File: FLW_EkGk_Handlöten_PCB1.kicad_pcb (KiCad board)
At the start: 2 copper layers, 120 x 60 mm, 72 parts, among them J10 Conn_01x02, J11 Conn_01x02, J12 Conn_01x02, J13 Conn_01x02, Q1 2SC4213, Q2 2N7002, Q60 2N7002, Q61 2N7002, Q62 2N7002, Q63 2N7002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

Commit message: continued
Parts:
- added LED66: SMLP36RGBNW3, NiksKiCadLibrary:LED_SMLP36_ROM, F.Cu at (104.9, 97.8)
- added LED67: SMLP36RGBNW3, NiksKiCadLibrary:LED_SMLP36_ROM, F.Cu at (104.9, 101.2)
- added R66: R, Resistor_SMD:R_1206_3216Metric, F.Cu at (101.6, 92.0)
- added R67: R, Resistor_SMD:R_1206_3216Metric, F.Cu at (104.8, 92.0)
- added R68: R, Resistor_SMD:R_1206_3216Metric, F.Cu at (108.1, 92.0)
- added R69: R, Resistor_SMD:R_1206_3216Metric, F.Cu at (101.6, 106.8)
- added R70: R, Resistor_SMD:R_1206_3216Metric, F.Cu at (104.8, 106.8)
- added R71: R, Resistor_SMD:R_1206_3216Metric, F.Cu at (108.1, 106.8)
- moved Q63 68.9 mm to (144.9, 94.8)
- moved Q64 68.5 mm to (144.9, 100.0)
- moved Q65 68.1 mm to (144.9, 105.1)
- moved Q60 57.4 mm to (139.5, 94.8)
- moved Q61 57.1 mm to (139.5, 100.0)
- moved Q62 56.8 mm to (139.5, 105.1)
- moved J13 46.1 mm to (99.5, 81.3), turned to 180 degrees
- moved J12 46.0 mm to (99.5, 74.9), turned to 180 degrees
- moved J11 46.0 mm to (99.5, 68.6), turned to 180 degrees
- moved J10 46.0 mm to (99.5, 62.2), turned to 180 degrees
- moved LED65 44.9 mm to (119.8, 97.0), turned to 150 degrees
- moved R62 44.8 mm to (130.5, 99.0), turned to -120 degrees
- moved R65 44.5 mm to (116.7, 99.5), turned to 60 degrees
- moved R61 44.2 mm to (126.9, 93.1), turned to -60 degrees
- moved R63 40.6 mm to (127.3, 105.1), turned to 180 degrees
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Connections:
- R60 pad 1: unconnected-(R60-Pad1) -> /Praxis 2/VDD_5V
- R61 pad 1: unconnected-(R61-Pad1) -> /Praxis 2/VDD_5V
- R62 pad 1: unconnected-(R62-Pad1) -> /Praxis 2/VDD_5V
- R63 pad 1: unconnected-(R63-Pad1) -> /Praxis 2/VDD_5V
- R64 pad 1: unconnected-(R64-Pad1) -> /Praxis 2/VDD_5V
- R65 pad 1: unconnected-(R65-Pad1) -> /Praxis 2/VDD_5V

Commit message: improved
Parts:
- removed D9: LED, LED_SMD:LED_PLCC-2_3x2mm_KA
- removed Q2: 2N7002, Package_TO_SOT_SMD:SOT-23
- removed R66, R67, R68, R69, R70, R71: R, Resistor_SMD:R_1206_3216Metric
- added LED68: LTST-E563CEGBW, NiksKiCadLibrary:LTSTE563CEGBW, F.Cu at (110.5, 104.8)
- added S60: MSS6-V-T_R, NiksKiCadLibrary:MSS6VTR, F.Cu at (160.9, 63.4)
- added SW60: MSS3-V-T/R, NiksKiCadLibrary:MSS3VTR, F.Cu at (208.7, 64.4)
- LED66, LED67: value SMLP36RGBNW3 -> LTST-E563CEGBW; footprint NiksKiCadLibrary:LED_SMLP36_ROM -> NiksKiCadLibrary:LTSTE563CEGBW
- moved U2 56.4 mm to (184.4, 85.6), turned to -90 degrees
- moved U5 23.2 mm to (199.0, 64.5)
- moved U1 10.3 mm to (185.1, 62.2)
- moved LED66 8.80 mm to (99.5, 104.8)
- moved Q1 8.52 mm to (171.2, 62.4)
- moved U3 8.35 mm to (176.8, 62.3)
- moved LED67 5.79 mm to (105.0, 95.5)
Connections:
- LED66 pad 1: Net-(LED66-Pad1) -> GND
- LED66 pad 2: Net-(LED66-Pad2) -> /LED_BUS_DIN
- LED66 pad 3: Net-(LED66-Pad3) -> Net-(LED66-DOUT)
- LED66 pad 4: GND -> /Praxis 2/VDD_5V
- LED67 pad 1: Net-(LED67-Pad1) -> GND
- LED67 pad 2: Net-(LED67-Pad2) -> Net-(LED66-DOUT)
- LED67 pad 4: GND -> /Praxis 2/VDD_5V
- U2 pad 11: unconnected-(U2A-GPIO8-Pad11) -> /LED_BUS_DIN
- U2 pad 13: unconnected-(U2B-GND-Pad13) -> GND
- U2 pad 18: unconnected-(U2B-GND-Pad18) -> GND
- U2 pad 21: /LEDR1 -> unconnected-(U2A-GPIO16-Pad21)
- U2 pad 22: /LEDG1 -> unconnected-(U2A-GPIO17-Pad22)
- U2 pad 23: unconnected-(U2B-GND-Pad23) -> GND
- U2 pad 24: /LEDB1 -> unconnected-(U2A-GPIO18-Pad24)
- U2 pad 25: /LEDR2 -> unconnected-(U2A-GPIO19-Pad25)
- U2 pad 26: /LEDG2 -> unconnected-(U2A-GPIO20-Pad26)
- U2 pad 27: /LEDB2 -> unconnected-(U2A-GPIO21-Pad27)
- U2 pad 28: unconnected-(U2B-GND-Pad28) -> GND
- U2 pad 3: unconnected-(U2B-GND-Pad3) -> GND
- U2 pad 33: unconnected-(U2B-AGND-Pad33) -> GND
- U2 pad 38: unconnected-(U2B-GND-Pad38) -> GND
- U2 pad 42: unconnected-(U2B-GND-Pad42) -> GND
- U2 pad 8: unconnected-(U2B-GND-Pad8) -> GND
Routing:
- net GNDD: track 4.38 -> 0.00 mm
- net (no net): track 0.00 -> 4.38 mm
- added copper zone on B.Cu, net (none)
- added copper zone on F.Cu, net GND
- removed copper zone on B.Cu, net GNDD
- removed copper zone on F.Cu, net GNDD

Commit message: Continued
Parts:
- removed Q1: 2SC4213, Package_TO_SOT_SMD:SOT-323_SC-70
- removed U1: LM555xM, Package_SO:SOIC-8_3.9x4.9mm_P1.27mm
- removed U5: ATmega16M1-A, Package_QFP:TQFP-32_7x7mm_P0.8mm
- added C60: 100n, Capacitor_SMD:C_1206_3216Metric, F.Cu at (184.9, 66.6)
- added IC60: HCF4094YM013TR, NiksKiCadLibrary:SOIC-16-SOIC127P600X175-16N, F.Cu at (160.2, 63.1)
- added IC61: HCF4094YM013TR, NiksKiCadLibrary:SOIC-16-SOIC127P600X175-16N, F.Cu at (170.2, 62.9)
- added R66: 10k, Resistor_SMD:R_1206_3216Metric, F.Cu at (201.4, 57.8)
- added SW61: B3U-3100P, NiksKiCadLibrary:SW_B3U-3100P_OMR, F.Cu at (201.6, 52.5)
- added U60: LM555xM, Package_SO:SOIC-8_3.9x4.9mm_P1.27mm, F.Cu at (185.1, 62.2)
- moved S60 35.9 mm to (196.8, 64.3)

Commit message: continued
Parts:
- removed C60: 100n, Capacitor_SMD:C_1206_3216Metric
- removed S60: MSS6-V-T_R, NiksKiCadLibrary:MSS6VTR
- removed U3: TPL5010, Package_TO_SOT_SMD:SOT-23-6
- removed U60: LM555xM, Package_SO:SOIC-8_3.9x4.9mm_P1.27mm
- added C61: 100n, Capacitor_SMD:C_1206_3216Metric, F.Cu at (121.8, 104.0)
- added C62: 100n, Capacitor_SMD:C_1206_3216Metric, F.Cu at (140.7, 103.9)
- added LED69: SML-LX1206SIC-TR, FabLabWintiLibrary:LED_SML-LX1206SIC-TR_LUM, F.Cu at (110.9, 91.7)
- added LED70: SML-LX1206SIC-TR, FabLabWintiLibrary:LED_SML-LX1206SIC-TR_LUM, F.Cu at (116.4, 91.7)
- added LED71: SML-LX1206SIC-TR, FabLabWintiLibrary:LED_SML-LX1206SIC-TR_LUM, F.Cu at (121.8, 91.7)
- added LED72: SML-LX1206SIC-TR, FabLabWintiLibrary:LED_SML-LX1206SIC-TR_LUM, F.Cu at (127.2, 91.7)
- added LED73: SML-LX1206SIC-TR, FabLabWintiLibrary:LED_SML-LX1206SIC-TR_LUM, F.Cu at (132.6, 91.7)
- added LED74: SML-LX1206SIC-TR, FabLabWintiLibrary:LED_SML-LX1206SIC-TR_LUM, F.Cu at (138.0, 91.5)
- added LED75: SML-LX1206SIC-TR, FabLabWintiLibrary:LED_SML-LX1206SIC-TR_LUM, F.Cu at (143.5, 91.7)
- added Q66: 2N7002, Package_TO_SOT_SMD:SOT-23, F.Cu at (110.8, 94.9)
- added Q67: 2N7002, Package_TO_SOT_SMD:SOT-23, F.Cu at (116.2, 94.9)
- added Q68: 2N7002, Package_TO_SOT_SMD:SOT-23, F.Cu at (121.6, 94.9)
- added Q69: 2N7002, Package_TO_SOT_SMD:SOT-23, F.Cu at (126.9, 94.9)
- added Q70: 2N7002, Package_TO_SOT_SMD:SOT-23, F.Cu at (132.3, 94.7)
- added Q71: 2N7002, Package_TO_SOT_SMD:SOT-23, F.Cu at (137.7, 94.9)
- added Q72: 2N7002, Package_TO_SOT_SMD:SOT-23, F.Cu at (143.1, 94.9)
- added R67: R, Resistor_SMD:R_1206_3216Metric, F.Cu at (110.9, 88.9)
- added R68: R, Resistor_SMD:R_1206_3216Metric, F.Cu at (116.3, 88.9)
- added R69: R, Resistor_SMD:R_1206_3216Metric, F.Cu at (121.7, 88.9)
- added R70: R, Resistor_SMD:R_1206_3216Metric, F.Cu at (127.1, 88.9)
- added R71: R, Resistor_SMD:R_1206_3216Metric, F.Cu at (132.5, 88.9)
- added R72: R, Resistor_SMD:R_1206_3216Metric, F.Cu at (137.9, 88.9)
- added R73: R, Resistor_SMD:R_1206_3216Metric, F.Cu at (143.3, 88.9)
- moved SW60 120.5 mm to (93.3, 99.3), turned to -90 degrees
- moved SW61 115.4 mm to (92.8, 90.9), turned to -90 degrees
- moved R66 101.0 mm to (105.7, 90.2), turned to -90 degrees
- moved LED64 73.3 mm to (181.3, 61.8)
- moved LED65 73.3 mm to (181.3, 57.3)
- moved R62 73.3 mm to (192.1, 59.2)
- moved LED60 73.3 mm to (185.2, 55.0)
- moved LED62 73.3 mm to (189.1, 61.8)
- moved LED63 73.3 mm to (185.2, 64.0)
- moved R63 73.3 mm to (188.8, 65.3)
- moved R65 73.3 mm to (178.2, 59.8)
- moved LED61 73.3 mm to (189.1, 57.3)
- moved R60 73.3 mm to (181.5, 53.6)
- moved R61 73.3 mm to (188.4, 53.4)
- moved R64 73.3 mm to (181.9, 65.7)
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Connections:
- net /LED1 renamed /led1
- net /LED2 renamed /led2
- net /LED3 renamed /led3
- net /LED4 renamed /led4
- net /LED5 renamed /led5
- net /LED6 renamed /led6
- net /LED_BUS_DIN renamed /led_bus_din
- IC60 pad 1: unconnected-(IC60-STROBE-Pad1) -> /strobe
- IC60 pad 14: unconnected-(IC60-Q5-Pad14) -> /Praxis 3/LED4
- IC60 pad 15: unconnected-(IC60-OUTPUT_ENABLE-Pad15) -> /en
- IC60 pad 16: unconnected-(IC60-VDD-Pad16) -> Net-(IC60-VDD)
- IC60 pad 2: Net-(IC60-DATA) -> /data
- IC60 pad 3: unconnected-(IC60-CLOCK-Pad3) -> /clk
- IC60 pad 4: unconnected-(IC60-Q1-Pad4) -> /Praxis 3/LED0
- IC60 pad 5: unconnected-(IC60-Q2-Pad5) -> /Praxis 3/LED1
- IC60 pad 6: unconnected-(IC60-Q3-Pad6) -> /Praxis 3/LED2
- IC60 pad 7: unconnected-(IC60-Q4-Pad7) -> /Praxis 3/LED3
- IC61 pad 1: unconnected-(IC61-STROBE-Pad1) -> /strobe
- IC61 pad 12: unconnected-(IC61-Q7-Pad12) -> /Praxis 3/LED14
- IC61 pad 15: unconnected-(IC61-OUTPUT_ENABLE-Pad15) -> /en
- IC61 pad 16: unconnected-(IC61-VDD-Pad16) -> Net-(IC61-VDD)
- IC61 pad 3: unconnected-(IC61-CLOCK-Pad3) -> /clk
- LED66 pad 4: /Praxis 2/VDD_5V -> /+5V
- LED67 pad 4: /Praxis 2/VDD_5V -> /+5V
- LED68 pad 4: /Praxis 2/VDD_5V -> /+5V
- R60 pad 1: /Praxis 2/VDD_5V -> /+5V
- R61 pad 1: /Praxis 2/VDD_5V -> /+5V
- R62 pad 1: /Praxis 2/VDD_5V -> /+5V
- R63 pad 1: /Praxis 2/VDD_5V -> /+5V
- R64 pad 1: /Praxis 2/VDD_5V -> /+5V
- R65 pad 1: /Praxis 2/VDD_5V -> /+5V
- R66 pad 1: /Praxis 3/+5V0 -> /+5V
- U2 pad 21: unconnected-(U2A-GPIO16-Pad21) -> /data
- U2 pad 22: unconnected-(U2A-GPIO17-Pad22) -> /clk
- U2 pad 24: unconnected-(U2A-GPIO18-Pad24) -> /strobe
- U2 pad 25: unconnected-(U2A-GPIO19-Pad25) -> /en
- U2 pad 40: unconnected-(U2B-VBUS-Pad40) -> /+5V
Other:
- board size 120 x 60 mm -> 120 x 66 mm

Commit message: Almost finished
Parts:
- added R74: 330R, Resistor_SMD:R_1206_3216Metric, F.Cu at (98.3, 88.0)
- added R75: 10k, Resistor_SMD:R_1206_3216Metric, F.Cu at (104.7, 103.6)
- added R76: 10k, Resistor_SMD:R_1206_3216Metric, F.Cu at (107.6, 103.6)
- added R77: 10k, Resistor_SMD:R_1206_3216Metric, F.Cu at (110.4, 103.6)
- added R78: 10k, Resistor_SMD:R_1206_3216Metric, F.Cu at (113.3, 103.6)
- added SW62: B3U-3100P, NiksKiCadLibrary:SW_B3U-3100P_OMR, F.Cu at (92.3, 92.0)
- added TP60: TestPoint, NiksKiCadLibrary:TestPointSimpleSMD, F.Cu at (137.7, 91.3)
- added TP61: TestPoint, NiksKiCadLibrary:TestPointSimpleSMD, F.Cu at (138.4, 88.5)
- added TP62: TestPoint, NiksKiCadLibrary:TestPointSimpleSMD, F.Cu at (140.8, 86.7)
- added TP63: TestPoint, NiksKiCadLibrary:TestPointSimpleSMD, F.Cu at (142.0, 89.3)
- added TP64: TestPoint, NiksKiCadLibrary:TestPointSimpleSMD, F.Cu at (141.5, 92.1)
- added TP65: TestPoint, NiksKiCadLibrary:TestPointSimpleSMD, F.Cu at (139.8, 94.5)
- added TP66: TestPoint, NiksKiCadLibrary:TestPointSimpleSMD, F.Cu at (140.8, 97.2)
- added TP67: TestPoint, NiksKiCadLibrary:TestPointSimpleSMD, F.Cu at (143.3, 95.5)
- added TP68: TestPoint, NiksKiCadLibrary:TestPointSimpleSMD, F.Cu at (144.6, 92.8)
- added TP69: TestPoint, NiksKiCadLibrary:TestPointSimpleSMD, F.Cu at (136.7, 108.8)
- R66: value 10k -> 330R
- moved C61 11.3 mm to (132.9, 105.7)
- moved IC60 10.7 mm to (125.6, 103.3)
- moved R66 8.44 mm to (98.3, 94.3), turned to 0 degrees
- moved C62 8.10 mm to (148.6, 105.5)
- moved IC61 7.28 mm to (141.0, 103.3)
- moved SW61 5.58 mm to (92.4, 85.3)
- moved LED75 5.17 mm to (148.6, 91.7)
- moved Q72 5.17 mm to (148.2, 94.9)
- moved R73 5.17 mm to (148.5, 88.9)
- moved LED73 4.14 mm to (128.5, 91.7)
- moved R72 4.14 mm to (133.8, 88.9)
- moved Q66 4.14 mm to (106.7, 94.8)
- moved Q68 4.14 mm to (117.4, 94.8)
- moved Q69 4.14 mm to (122.8, 94.8)
- moved R69 4.14 mm to (117.6, 88.9)
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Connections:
- net /Praxis 3/LED0 renamed /Praxis 3/led0
- net /Praxis 3/LED1 renamed /Praxis 3/led1
- net /Praxis 3/LED2 renamed /Praxis 3/led2
- net /Praxis 3/LED3 renamed /Praxis 3/led3
- net /Praxis 3/LED4 renamed /Praxis 3/led4
- C61 pad 1: Net-(IC60-VDD) -> /Praxis 3/+5v0
- C62 pad 1: Net-(IC61-VDD) -> /Praxis 3/+5v0
- IC60 pad 11: unconnected-(IC60-Q8-Pad11) -> Net-(IC60-Q8)
- IC60 pad 12: unconnected-(IC60-Q7-Pad12) -> Net-(IC60-Q7)
- IC60 pad 13: unconnected-(IC60-Q6-Pad13) -> /Praxis 3/led5
- IC60 pad 16: Net-(IC60-VDD) -> /Praxis 3/+5v0
- IC61 pad 11: unconnected-(IC61-Q8-Pad11) -> /Praxis 3/led15
- IC61 pad 12: /Praxis 3/LED14 -> Net-(IC61-Q7)
- IC61 pad 13: unconnected-(IC61-Q6-Pad13) -> Net-(IC61-Q6)
- IC61 pad 14: unconnected-(IC61-Q5-Pad14) -> Net-(IC61-Q5)
- IC61 pad 16: Net-(IC61-VDD) -> /Praxis 3/+5v0
- IC61 pad 4: unconnected-(IC61-Q1-Pad4) -> Net-(IC61-Q1)
- IC61 pad 5: unconnected-(IC61-Q2-Pad5) -> Net-(IC61-Q2)
- IC61 pad 6: unconnected-(IC61-Q3-Pad6) -> Net-(IC61-Q3)
- IC61 pad 7: unconnected-(IC61-Q4-Pad7) -> Net-(IC61-Q4)
- IC61 pad 9: unconnected-(IC61-QS-Pad9) -> Net-(IC61-QS)
- Q71 pad 1: /Praxis 3/LED14 -> /Praxis 3/led5
- Q72 pad 1: /Praxis 3/LED15 -> /Praxis 3/led15
- R66 pad 1: /+5V -> Net-(R66-Pad1)
- R66 pad 2: /Praxis 3/nRST -> /data
- R67 pad 1: /+5V -> /Praxis 3/+5v0
- R68 pad 1: /+5V -> /Praxis 3/+5v0
- R69 pad 1: /+5V -> /Praxis 3/+5v0
- R70 pad 1: /+5V -> /Praxis 3/+5v0
- R71 pad 1: /+5V -> /Praxis 3/+5v0
- R72 pad 1: /+5V -> /Praxis 3/+5v0
- R73 pad 1: /+5V -> /Praxis 3/+5v0
- SW60 pad A1: (no net) -> /Praxis 3/+5v0
- SW60 pad B1: (no net) -> /+5V
- SW60 pad C1: (no net) -> unconnected-(SW60-3-PadC1)
- SW60 pad MP1: (no net) -> GND
- SW60 pad MP2: (no net) -> GND
- SW60 pad MP3: (no net) -> GND
- SW60 pad MP4: (no net) -> GND
- SW61 pad 2: /Praxis 3/nRST -> Net-(R74-Pad1)
- SW61 pad 3: unconnected-(SW61-Sense-Pad3) -> GND
- U2 pad 36: unconnected-(U2B-3V3-Pad36) -> /+3V3
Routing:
- net /+5V: track 0.00 -> 231.2 mm, vias 0 -> 2
- net /Praxis 3/+5v0: track 0.00 -> 127.6 mm
- net /+3V3: track 0.00 -> 106.1 mm
- net /clk: track 0.00 -> 85.7 mm, vias 0 -> 4
- net /data: track 0.00 -> 76.1 mm, vias 0 -> 3
- net /en: track 0.00 -> 74.1 mm, vias 0 -> 3
- net /strobe: track 0.00 -> 67.0 mm, vias 0 -> 4
- net Net-(J10-Pin_2): track 0.00 -> 59.3 mm
- net Net-(J13-Pin_1): track 0.00 -> 59.0 mm
- net Net-(J12-Pin_2): track 0.00 -> 58.7 mm
- net Net-(J11-Pin_1): track 0.00 -> 57.2 mm
- net Net-(J13-Pin_2): track 0.00 -> 50.3 mm
- net Net-(J11-Pin_2): track 0.00 -> 50.1 mm
- net /led_bus_din: track 0.00 -> 42.4 mm, vias 0 -> 2
- net /led2: track 0.00 -> 36.8 mm
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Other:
- board text added: "0"
- board text added: "1"
- board text added: "15"
- board text added: "2"
- board text added: "3"
- board text added: "4"
- board text added: "5"
- board text added: "LED0"
- board text added: "LED1"
- board text added: "LED2"
- board text added: "LED3"
- board text added: "LED4"
- board text added: "LED5"
- board text added: "Praxis 3 - Verschiedenes"
- board text added: "QS"
- board text added: "RGB0"
- board text added: "RGB1"
- board text added: "RGB2"
- board text removed: "Praxis 3 - Verschiedene Gehäusetypen"

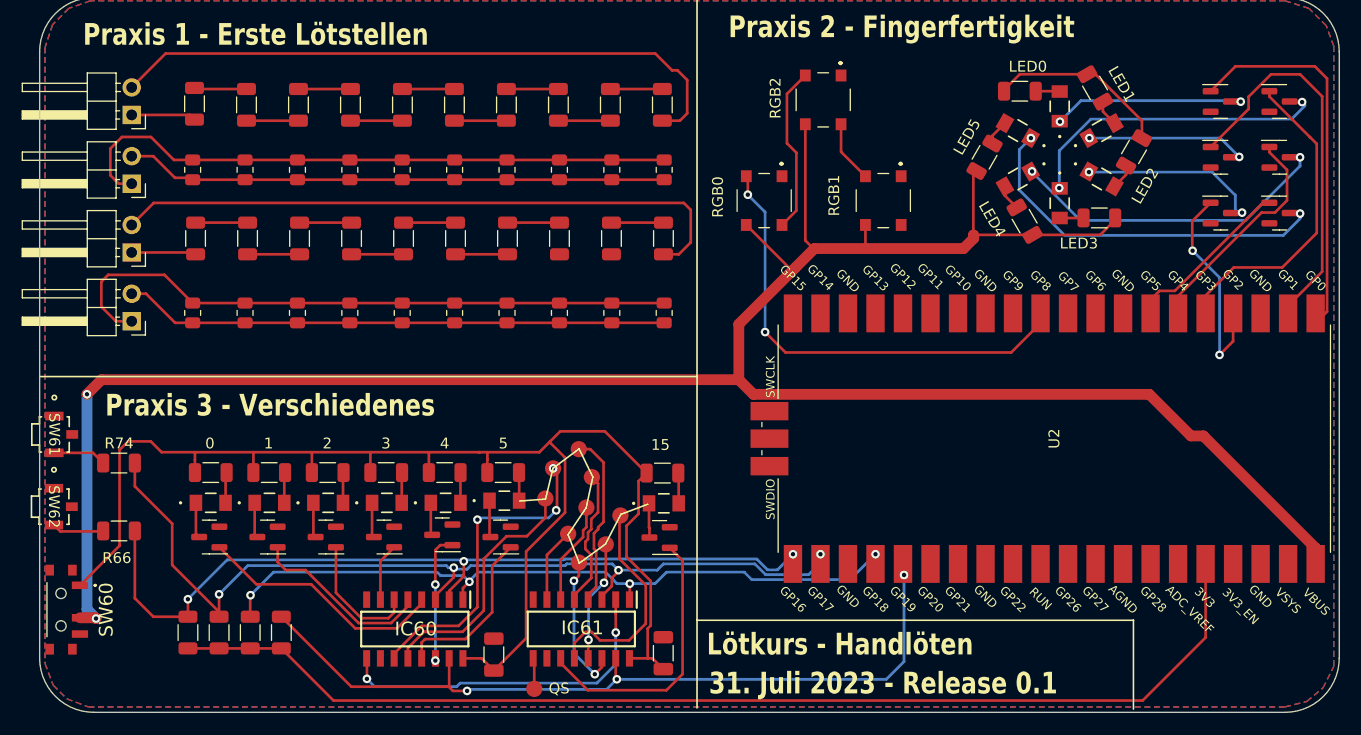
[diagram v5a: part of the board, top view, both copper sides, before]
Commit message: Cleaned up some warnings
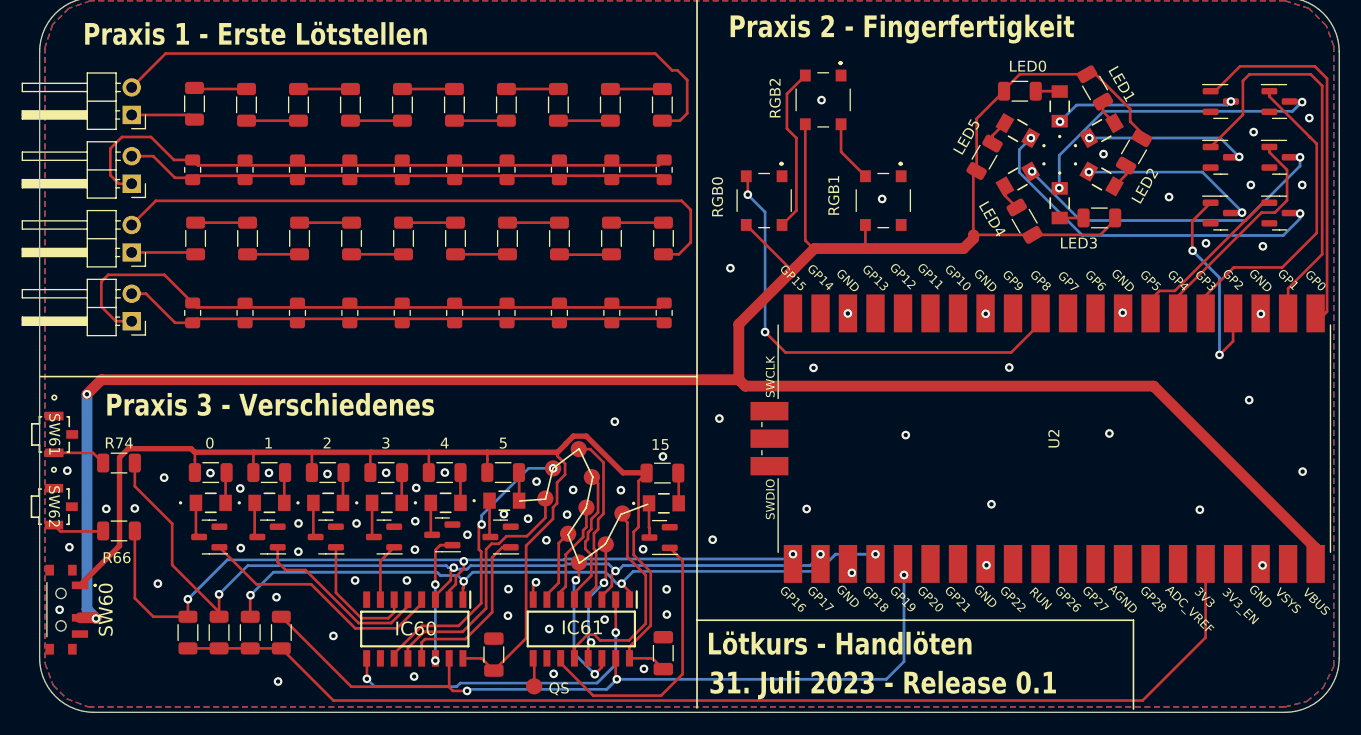
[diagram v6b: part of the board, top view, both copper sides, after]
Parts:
- moved TP68 0.26 mm to (144.8, 92.6)
- moved TP69 0.24 mm to (136.7, 108.6)
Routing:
- net /+5V: track 231.2 -> 239.6 mm
- net Net-(R37-Pad1): track 0.00 -> 4.83 mm
- net /Praxis 3/+5v0: track 127.6 -> 125.0 mm
- net Net-(IC60-Q8): track 29.7 -> 27.1 mm, vias 3 -> 2
- net Net-(Q60-D): track 18.5 -> 16.6 mm
- net /led2: track 36.8 -> 38.6 mm
- net GND: track 0.00 -> 1.71 mm, vias 0 -> 75
- net /clk: track 85.7 -> 84.3 mm
- net Net-(Q63-D): track 29.5 -> 28.3 mm
- net Net-(Q65-D): track 35.0 -> 34.1 mm
- net /data: track 76.1 -> 75.3 mm
- net Net-(Q62-D): track 17.6 -> 16.8 mm
- net /strobe: track 67.0 -> 66.4 mm
- net Net-(IC61-Q7): track 20.4 -> 19.9 mm
- added copper zone on B.Cu, net GND
- removed copper zone on B.Cu, net (none)

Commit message: Removed Aisler Tag
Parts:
- removed the G*** at (118.0, 85.5)
- moved G*** 33.6 mm to (151.2, 77.1)
- moved G*** 8.30 mm to (151.1, 57.7)
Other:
- board text added: "PCB designed by FABLAB Winti using KiCad - Produced by aisler.net in Germany"
- board text removed: "PCB designed by FABLAB Winti using KiCad - Produced by Aisler in Germany"
- board text removed: "www.aisler.net"

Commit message: Last changes
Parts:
- SW60: value MSS3-V-T/R -> MSS6-V-T_R; footprint NiksKiCadLibrary:MSS3VTR -> NiksKiCadLibrary:MSS6VTR
- moved SW60 3.41 mm to (96.3, 102.4)
- moved R74 2.92 mm to (101.2, 88.6)
- moved R66 2.88 mm to (101.0, 95.3)
- moved TP69 0.43 mm to (136.6, 108.2)
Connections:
- R75 pad 1: /+3V3 -> /Praxis 3/+3v3
- R76 pad 1: /+3V3 -> /Praxis 3/+3v3
- R77 pad 1: /+3V3 -> /Praxis 3/+3v3
- R78 pad 1: /+3V3 -> /Praxis 3/+3v3
- SW60 pad A1: /Praxis 3/+5v0 -> /Praxis 3/+3v3
- SW60 pad B1: /+5V -> /+3V3
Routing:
- net /Praxis 3/+3v3: track 0.00 -> 16.6 mm
- net /+3V3: track 106.1 -> 112.5 mm
- net /led3: track 19.3 -> 13.4 mm
- net /data: track 75.3 -> 71.3 mm
- net Net-(R74-Pad1): track 4.90 -> 8.75 mm
- net /Praxis 3/+5v0: track 125.0 -> 128.1 mm, vias 0 -> 2
- net Net-(R66-Pad1): track 4.80 -> 7.88 mm
- net Net-(LED66-DOUT): track 15.4 -> 16.9 mm
- net /clk: track 84.3 -> 83.0 mm
- net /Praxis 3/led1: track 17.0 -> 16.2 mm
- net Net-(Q65-D): track 34.1 -> 33.4 mm
- net Net-(IC60-QS): track 32.0 -> 32.6 mm
- net /en: track 74.1 -> 74.6 mm
- net GND: vias 75 -> 74
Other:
- board text added: "21. November 2023 - Release 1.0"
- board text added: "Clock Pulse"
- board text added: "Data"
- board text added: "Released = 1 Pressed = 0"
- board text removed: "31. Juli 2023 - Release 0.1"
